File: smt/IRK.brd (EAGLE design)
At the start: 142.9 x 39.7 mm, 40 parts, among them IC1 PIC18F25K50, Q1 MMBT2222A, Q2 2N7002, Q3 2N7002, Q4 TSOP4838, Q5 MMBT3906

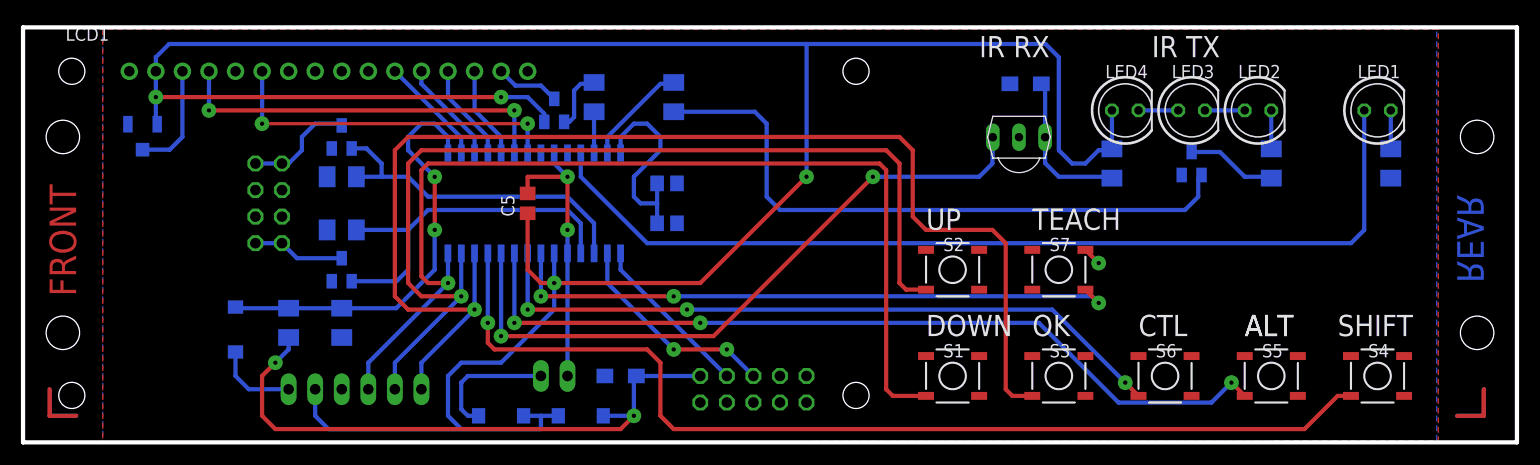
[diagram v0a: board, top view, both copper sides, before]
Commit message: Reworked project structure to accommodate SMD and THT versions.
The orginal Through Hole Technology (THT) version is now stored
in the tht/ directory and the new Surface Mount Technology (SMT)
version is stored in the smt/ directory.
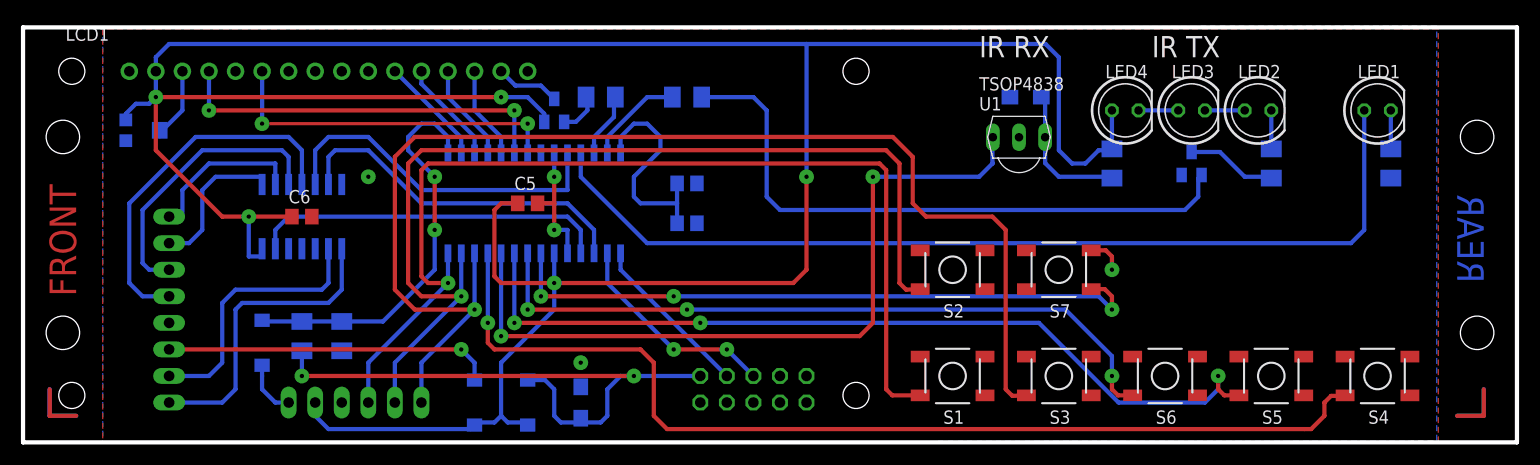
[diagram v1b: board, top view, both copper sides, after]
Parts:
- removed JP1: PWR/RST, pinhead:2X04
- removed JP4: STANDBY, pinhead:1X02
- removed Q3: 2N7002, transistors_gaui:SOT23
- removed Q4: TSOP4838, tsop:TSOP18XX
- removed Q5: MMBT3906, transistor-pnp:SOT23-BEC
- removed R6, R7: 10k, rcl:M1206
- added C6: 100nF, rcl:C0805
- added IC2: MAX4066ESD, irk:SO14
- added JP5: SWITCHES, pinhead:1X08
- added U1: TSOP4838, irk:TSOP18XX
- D1, D2, D3: device SparkFun-DiscreteSemi:SMA-DIODE -> irk:SMA-DIODE
- LCD1: value TUXGR_16X2_R2 -> HD44780; device offboard:TUXGR_16X2_R2 -> irk:LCD_16X2
- LED1: value ACTVITY -> ACTIVITY
- LED3, LED4: value (none) -> (none)
- Q1: device transistor:SOT23-BEC -> irk:SOT23
- Q2: value 2N7002 -> MMBT3906; device transistors_gaui:SOT23 -> irk:SOT23
- S1, S2, S3, S4, S5, S6, S7: device SparkFun-Electromechanical:TACTILE_SWITCH_SMD -> irk:PTH525-SM10
- VR1: device pot:3223W -> irk:3303W
- moved Q2 20.5 mm to (50.8, 31.8)
- moved D3 5.24 mm to (48.3, 3.81), turned to 270 degrees
- moved C1 4.58 mm to (53.3, 3.81), turned to 90 degrees
- moved D1 2.84 mm to (43.2, 3.81), turned to 270 degrees
- moved D2 2.84 mm to (22.9, 9.53)
- moved C3 1.91 mm to (63.5, 24.8)
- moved C4 1.91 mm to (63.5, 21.0)
- moved R9 1.80 mm to (26.7, 10.2)
- moved R5 1.27 mm to (63.5, 33.0), turned to 0 degrees
- moved JP2 1.27 mm to (31.8, 3.81)
- moved R1 1.27 mm to (30.5, 10.2)
- moved C2 1.27 mm to (95.9, 33.0)
- moved R8 0.63 mm to (55.2, 33.0), turned to 0 degrees
- moved VR1 0.63 mm to (11.4, 29.8), turned to 90 degrees
- turned C5 to 0 degrees
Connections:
- removed net N$32: D1.A, JP4.1
- removed net N$37: IC1.17, Q2.1, R6.2
- removed net N$9: IC1.18, Q3.1, R7.2
- new net AUX: IC1.10, IC2.5
- new net N$33: IC2.4, JP5.4
- new net N$35: IC2.3, JP5.3
- new net N$39: IC2.9, JP5.7
- new net N$40: IC2.8, JP5.8
- new net PWR: IC1.17, IC2.6
- new net RST: IC1.18, IC2.13
- new net VSB: D1.A, JP5.6
- net +5V: now also C6.1, D1.K, D3.K, IC2.14, Q2.2; no longer D1.C, D3.C, Q5.E
- net GND: now also C6.2, IC2.12, IC2.7, JP5.5, Q1.2, U1.GND; no longer JP1.3, JP1.4, JP1.5, JP1.6, JP4.2, Q1.E, Q2.2, Q3.2, Q4.GND, R6.1, R7.1
- net N$10: now also U1.OUT; no longer Q4.OUT
- net N$11: now also IC2.2, JP5.1; no longer JP1.1, JP1.2, Q3.3
- net N$22: now also IC2.1, JP5.2; no longer JP1.7, JP1.8, Q2.3
- net N$29: now also Q1.1; no longer Q1.B
- net N$30: now also Q1.3; no longer Q1.C
- net N$31: now also Q2.3; no longer Q5.C
- net N$36: now also Q2.1; no longer Q5.B
- net N$50: now also U1.VCC; no longer Q4.VCC
- net N$8: now also D2.K; no longer D2.C
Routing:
- net N$9: track 35.3 -> 0.00 mm
- net N$33: track 0.00 -> 34.9 mm
- net RST: track 0.00 -> 34.3 mm
- net PWR: track 0.00 -> 33.7 mm
- net AUX: track 0.00 -> 33.5 mm
- net N$37: track 32.2 -> 0.00 mm
- net VSB: track 0.00 -> 31.4 mm, vias 0 -> 1
- net N$40: track 0.00 -> 29.4 mm
- net N$35: track 0.00 -> 27.1 mm
- net +5V: track 254.4 -> 281.0 mm, vias 4 -> 5
- net N$39: track 0.00 -> 25.5 mm
- net GND: track 29.0 -> 15.9 mm, vias 3 -> 5
- net N$32: track 12.3 -> 0.00 mm
- net N$10: track 64.3 -> 72.6 mm
- net N$11: track 8.85 -> 15.8 mm
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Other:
- board text removed: "ALT"
- board text removed: "CTL"
- board text removed: "DOWN"
- board text removed: "ICSP"
- board text removed: "OK"
- board text removed: "SHIFT"
- board text removed: "TEACH"
- board text removed: "UP"

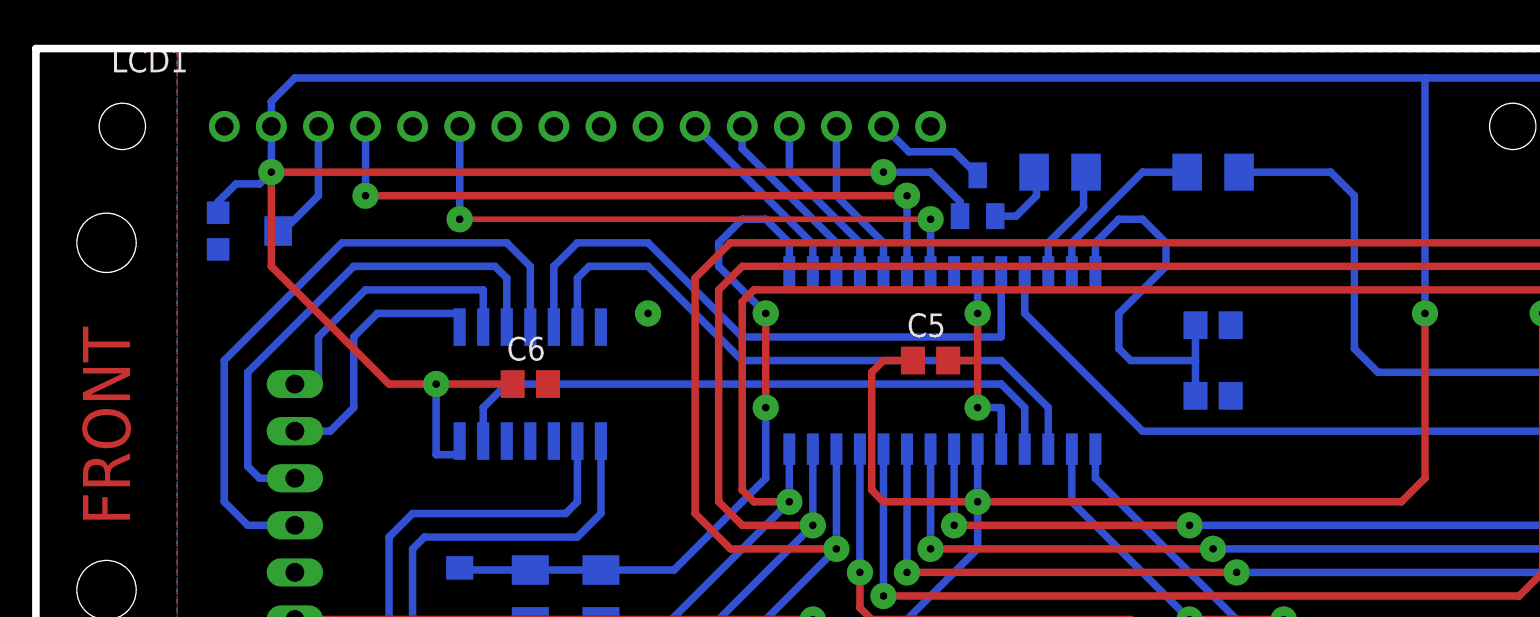
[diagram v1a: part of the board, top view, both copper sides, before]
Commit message: Made cosmetic changes.
1. Used the HID Report Descriptor Decoder (http://sourceforge.net/projects/hidrdd/)
   to document the report descriptor meaning.
2. Changed the trimpot in IRK.lbr so that it has a tRestrict under it (this
   prevents copper traces being routed under the metal part of the trimpot).
3. Improved the routing of the track for the 100nF capacitor under the PIC18F25K50
   chip.
4. For the LCD library initialisation, used LAT registers instead of PORT registers
   (this probably doesn't make any difference to the operation).
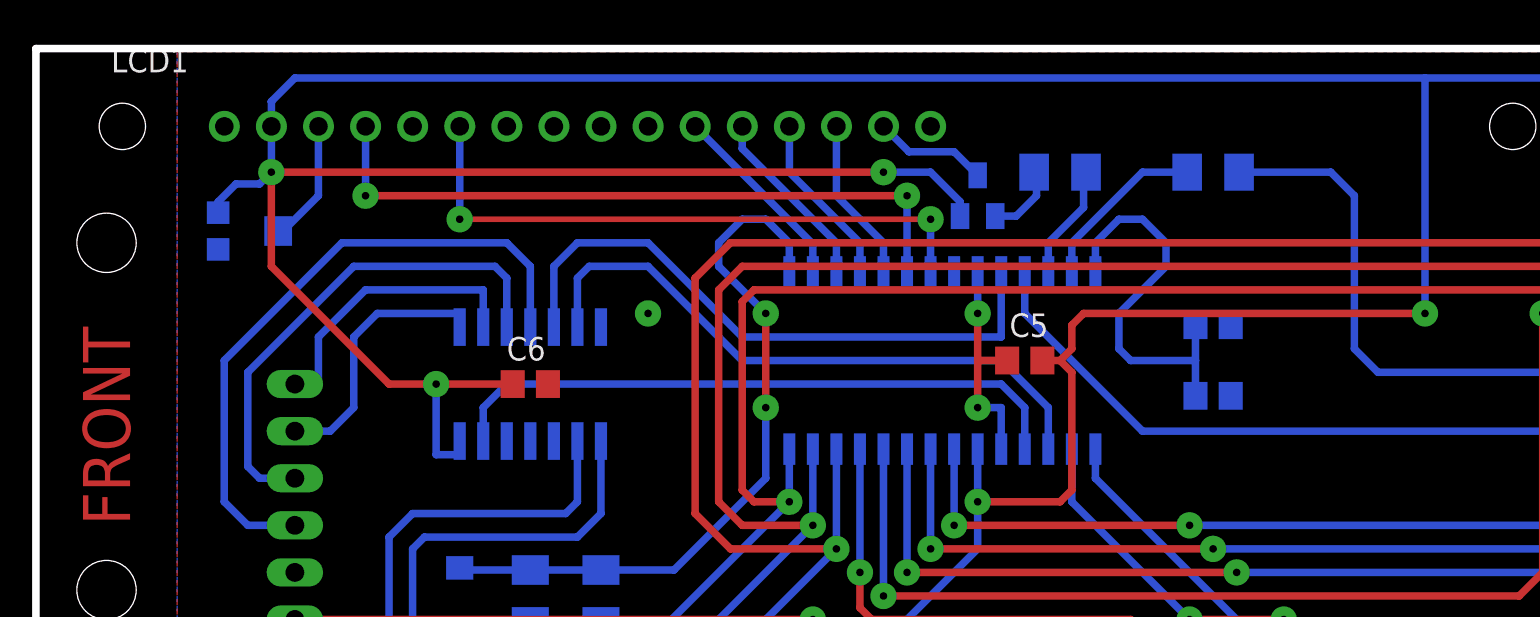
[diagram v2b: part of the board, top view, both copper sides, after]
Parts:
- moved C5 5.08 mm to (53.3, 22.9), turned to 180 degrees
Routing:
- net +5V: track 281.0 -> 267.6 mm
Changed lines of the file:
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@@
 <layer number="19" name="Unrouted" color="6" fill="1" visible="yes" active="yes"/>
 <layer number="20" name="Dimension" color="15" fill="1" visible="yes" active="yes"/>
-<layer number="21" name="tPlace" color="15" fill="1" visible="no" active="yes"/>
+<layer number="21" name="tPlace" color="15" fill="1" visible="yes" active="yes"/>
 <layer number="22" name="bPlace" color="23" fill="1" visible="yes" active="yes"/>
-<layer number="23" name="tOrigins" color="15" fill="1" visible="no" active="yes"/>
+<layer number="23" name="tOrigins" color="15" fill="1" visible="yes" active="yes"/>
 <layer number="24" name="bOrigins" color="23" fill="1" visible="yes" active="yes"/>
-<layer number="25" name="tNames" color="15" fill="1" visible="no" active="yes"/>
+<layer number="25" name="tNames" color="15" fill="1" visible="yes" active="yes"/>
 <layer number="26" name="bNames" color="23" fill="1" visible="yes" active="yes"/>
-<layer number="27" name="tValues" color="15" fill="1" visible="no" active="yes"/>
+<layer number="27" name="tValues" color="15" fill="1" visible="yes" active="yes"/>
 <layer number="28" name="bValues" color="23" fill="1" visible="yes" active="yes"/>
 <layer number="29" name="tStop" color="7" fill="3" visible="no" active="yes"/>
@@
 <layer number="39" name="tKeepout" color="3" fill="11" visible="no" active="yes"/>
 <layer number="40" name="bKeepout" color="1" fill="11" visible="no" active="yes"/>
-<layer number="41" name="tRestrict" color="14" fill="11" visible="no" active="yes"/>
-<layer number="42" name="bRestrict" color="6" fill="11" visible="no" active="yes"/>
+<layer number="41" name="tRestrict" color="14" fill="11" visible="yes" active="yes"/>
+<layer number="42" name="bRestrict" color="6" fill="11" visible="yes" active="yes"/>
 <layer number="43" name="vRestrict" color="2" fill="10" visible="no" active="yes"/>
 <layer number="44" name="Drills" color="7" fill="1" visible="no" active="yes"/>
-<layer number="45" name="Holes" color="7" fill="1" visible="yes" active="yes"/>
+<layer number="45" name="Holes" color="7" fill="1" visible="no" active="yes"/>
 <layer number="46" name="Milling" color="3" fill="1" visible="no" active="yes"/>
 <layer number="47" name="Measures" color="7" fill="1" visible="no" active="yes"/>
@@
 <layer number="50" name="dxf" color="7" fill="1" visible="no" active="yes"/>
 <layer number="51" name="tDocu" color="7" fill="1" visible="no" active="yes"/>
-<layer number="52" name="bDocu" color="7" fill="1" visible="yes" active="yes"/>
+<layer number="52" name="bDocu" color="7" fill="1" visible="no" active="yes"/>
 <layer number="53" name="tGND_GNDA" color="7" fill="9" visible="no" active="no"/>
 <layer number="54" name="bGND_GNDA" color="1" fill="9" visible="no" active="no"/>
@@
 <rectangle x1="21.59" y1="8.89" x2="24.13" y2="10.16" layer="42"/>
 <rectangle x1="41.91" y1="2.54" x2="44.45" y2="5.08" layer="42"/>
-<rectangle x1="10.795" y1="29.21" x2="12.065" y2="31.75" layer="42"/>
 <text x="24.13" y="6.35" size="2.032" layer="122" font="vector" rot="MR90">VPP</text>
 <text x="24.765" y="1.27" size="1.27" layer="122" font="vector" rot="MR0">1</text>
@@
 <attribute name="VALUE" x="64.77" y="30.48" size="1.27" layer="28" font="vector" rot="MR0"/>
 </element>
-<element name="C5" library="rcl" package="C0805" value="100nF" x="48.26" y="22.86" smashed="yes">
-<attribute name="NAME" x="46.99" y="24.13" size="1.27" layer="25" font="vector" ratio="10"/>
-<attribute name="VALUE" x="46.99" y="20.32" size="1.27" layer="27"/>
+<element name="C5" library="rcl" package="C0805" value="100nF" x="53.34" y="22.86" smashed="yes" rot="R180">
+<attribute name="NAME" x="54.61" y="25.4" size="1.27" layer="25" font="vector" ratio="10" rot="R180"/>
+<attribute name="VALUE" x="57.15" y="21.59" size="1.27" layer="27" font="vector" rot="R180"/>
 </element>
 <element name="C2" library="rcl" package="SMC_A" value="4.7uF" x="95.885" y="33.02" smashed="yes" rot="MR0">
@@
 <attribute name="VALUE" x="50.546" y="7.874" size="1.27" layer="28" font="vector" rot="MR90"/>
 </element>
-<element name="LCD1" library="irk" package="LCD_16X2" value="HD44780" x="42.164" y="19.9898"/>
+<element name="LCD1" library="irk" package="LCD_16X2" value="HD44780" x="42.164" y="19.9898" smashed="yes">
+<attribute name="NAME" x="4.064" y="38.4048" size="1.27" layer="25" font="vector"/>
+<attribute name="VALUE" x="42.799" y="38.4048" size="1.27" layer="27" font="vector"/>
+</element>
 <element name="JP5" library="pinhead" package="1X08" value="SWITCHES" x="13.97" y="12.7" smashed="yes" rot="MR270">
 <attribute name="NAME" x="12.6238" y="24.2062" size="1.27" layer="26" font="vector" rot="MR180"/>
@@
 <attribute name="NAME" x="21.971" y="25.908" size="1.27" layer="26" font="vector" rot="MR270"/>
 </element>
-<element name="C6" library="rcl" package="C0805" value="100nF" x="26.67" y="21.59"/>
+<element name="C6" library="rcl" package="C0805" value="100nF" x="26.67" y="21.59" smashed="yes">
+<attribute name="NAME" x="25.4" y="22.86" size="1.27" layer="25" font="vector"/>
+<attribute name="VALUE" x="25.4" y="19.05" size="1.27" layer="27" font="vector"/>
+</element>
 <element name="VR1" library="irk" package="3303W" value="10k" x="11.43" y="29.845" rot="MR90"/>
 <element name="U1" library="irk" package="TSOP18XX" value="TSOP4838" x="95.25" y="29.21" smashed="yes">
@@
 <wire x1="97.79" y1="38.1" x2="74.93" y2="38.1" width="0.4064" layer="16"/>
 <wire x1="99.06" y1="36.83" x2="97.79" y2="38.1" width="0.4064" layer="16"/>
-<wire x1="73.66" y1="15.24" x2="50.8" y2="15.24" width="0.4064" layer="1"/>
-<wire x1="74.93" y1="25.4" x2="74.93" y2="16.51" width="0.4064" layer="1"/>
-<wire x1="74.93" y1="16.51" x2="73.66" y2="15.24" width="0.4064" layer="1"/>
 <wire x1="74.93" y1="38.1" x2="74.93" y2="25.4" width="0.4064" layer="16"/>
 <via x="50.8" y="15.24" extent="1-16" drill="0.4064"/>
@@
 <wire x1="22.86" y1="17.78" x2="21.59" y2="17.78" width="0.4064" layer="16"/>
 <wire x1="21.59" y1="17.78" x2="21.59" y2="21.59" width="0.4064" layer="16"/>
-<wire x1="47.31" y1="22.86" x2="45.72" y2="22.86" width="0.4064" layer="1"/>
-<wire x1="45.72" y1="22.86" x2="45.085" y2="22.225" width="0.4064" layer="1"/>
-<wire x1="45.085" y1="22.225" x2="45.085" y2="15.875" width="0.4064" layer="1"/>
-<wire x1="45.085" y1="15.875" x2="45.72" y2="15.24" width="0.4064" layer="1"/>
-<wire x1="45.72" y1="15.24" x2="50.8" y2="15.24" width="0.4064" layer="1"/>
 <wire x1="50.8" y1="15.24" x2="50.8" y2="12.7" width="0.4064" layer="16"/>
 <contactref element="VR1" pad="3"/>
@@
 <wire x1="46.355" y1="1.905" x2="48.015" y2="1.905" width="0.4064" layer="16"/>
 <wire x1="48.015" y1="1.905" x2="48.26" y2="1.66" width="0.4064" layer="16"/>
+<wire x1="55.245" y1="22.86" x2="55.88" y2="23.495" width="0.4064" layer="1"/>
+<wire x1="55.88" y1="23.495" x2="55.88" y2="24.765" width="0.4064" layer="1"/>
+<wire x1="55.88" y1="24.765" x2="56.515" y2="25.4" width="0.4064" layer="1"/>
+<wire x1="56.515" y1="25.4" x2="74.93" y2="25.4" width="0.4064" layer="1"/>
+<wire x1="54.29" y1="22.86" x2="55.245" y2="22.86" width="0.4064" layer="1"/>
+<wire x1="55.245" y1="22.86" x2="55.88" y2="22.225" width="0.4064" layer="1"/>
+<wire x1="55.88" y1="22.225" x2="55.88" y2="15.875" width="0.4064" layer="1"/>
+<wire x1="55.88" y1="15.875" x2="55.245" y2="15.24" width="0.4064" layer="1"/>
+<wire x1="55.245" y1="15.24" x2="50.8" y2="15.24" width="0.4064" layer="1"/>
 </signal>
 <signal name="N$7">
@@
 <wire x1="50.8" y1="20.32" x2="52.07" y2="20.32" width="0.4064" layer="16"/>
 <wire x1="52.07" y1="20.32" x2="52.07" y2="18.08" width="0.4064" layer="16"/>
-<wire x1="50.8" y1="25.4" x2="50.8" y2="22.86" width="0.4064" layer="1"/>
-<wire x1="50.8" y1="22.86" x2="50.8" y2="20.32" width="0.4064" layer="1"/>
+<wire x1="50.8" y1="25.4" x2="50.8" y2="22.86" width="0" layer="19" extent="1-16"/>
+<wire x1="50.8" y1="25.4" x2="50.8" y2="22.86" width="0" layer="19" extent="1-16"/>
 <polygon width="0.4064" layer="16" isolate="0.6096">
 <vertex x="7.62" y="0"/>
@@
 <contactref element="LCD1" pad="10"/>
 <contactref element="LCD1" pad="16"/>
+<wire x1="50.8" y1="25.4" x2="50.8" y2="22.86" width="0.4064" layer="1"/>
+<wire x1="50.8" y1="22.86" x2="50.8" y2="20.32" width="0.4064" layer="1"/>
 <wire x1="50.8" y1="27.64" x2="50.8" y2="25.4" width="0.4064" layer="16"/>
 <via x="33.02" y="25.4" extent="1-16" drill="0.4064" diameter="0.8128"/>
@@
 <contactref element="C6" pad="2"/>
 <contactref element="IC2" pad="7"/>
-<wire x1="49.21" y1="22.86" x2="50.8" y2="22.86" width="0.4064" layer="1"/>
 <via x="53.34" y="7.62" extent="1-16" drill="0.4064" diameter="0.8128"/>
 <contactref element="VR1" pad="1"/>
@@
 <wire x1="103.5558" y1="18.3642" x2="104.14" y2="17.78" width="0.4064" layer="1"/>
 <wire x1="104.14" y1="17.78" x2="104.14" y2="16.51" width="0.4064" layer="1"/>
+<wire x1="52.39" y1="22.86" x2="50.8" y2="22.86" width="0.4064" layer="1"/>
 </signal>
 <signal name="N$50">
